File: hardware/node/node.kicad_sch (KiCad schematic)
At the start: 51 parts, among them IC1 MCP73844-840I_MS, IC2 NEO-M9N-00B, J1 USB_C_Receptacle, J2 OMEGA2_HEADER, Q1 IRF7404, Q2 AO3400A, Q3 S8550, SW1 SW_POWER, U1 MT3608, U2 AP63203WU, U3 ADS1115IDGS, U4 Omega2S

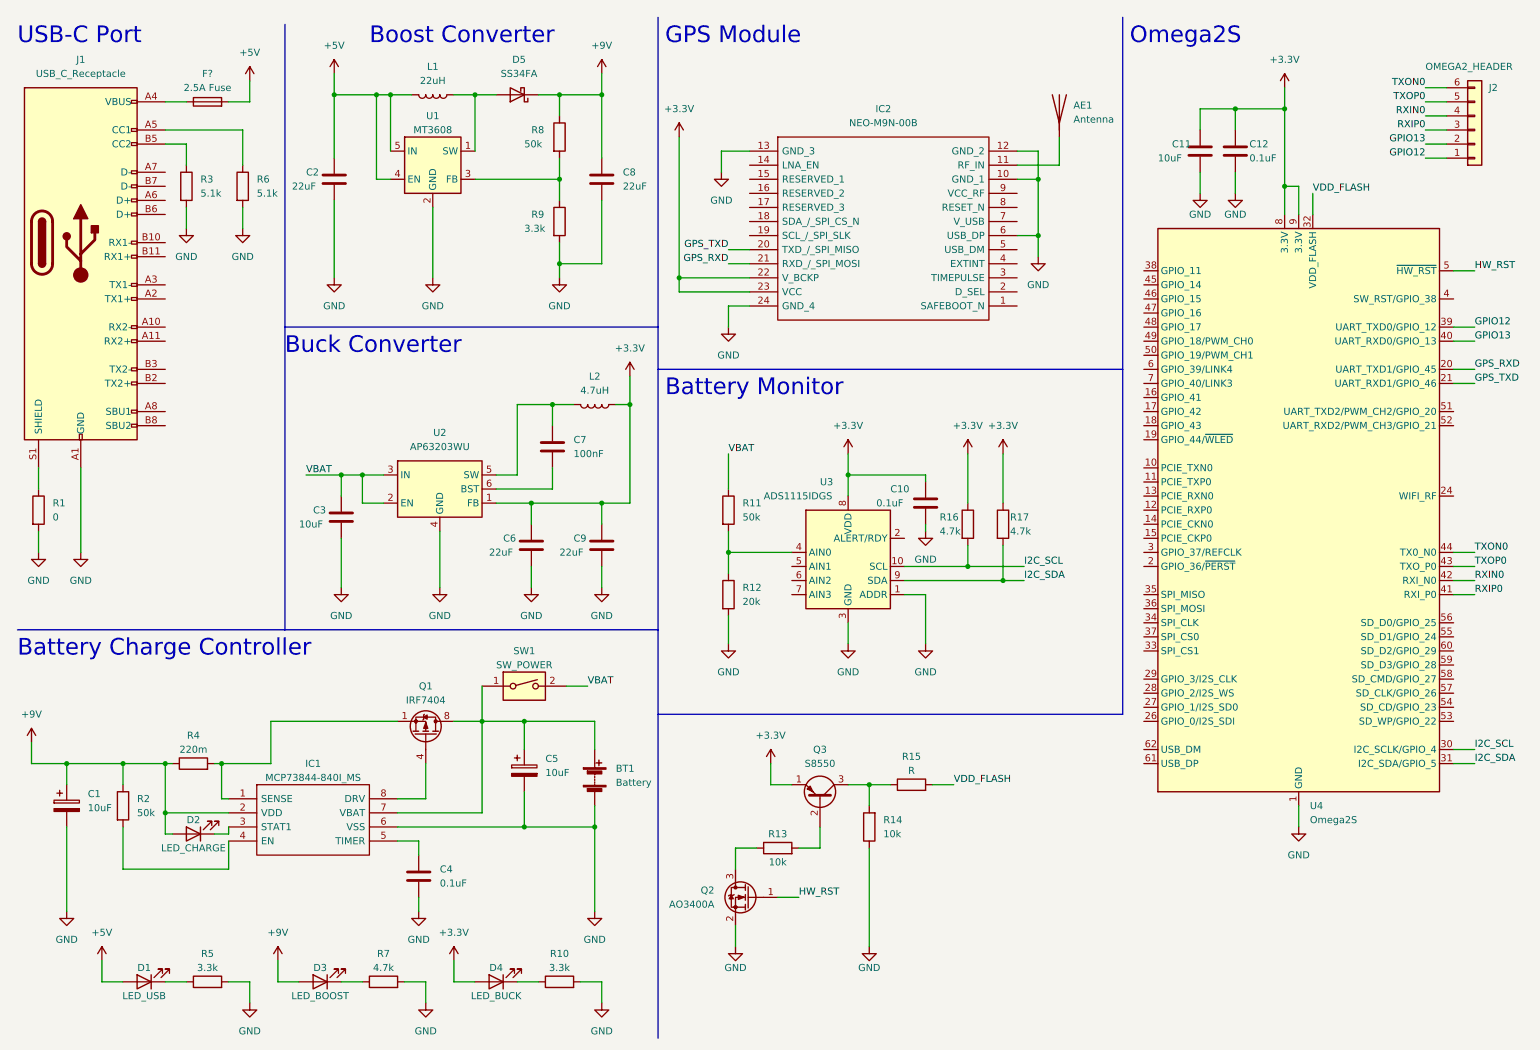
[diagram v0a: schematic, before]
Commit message: fix schematic naming, remove hard reset circuit
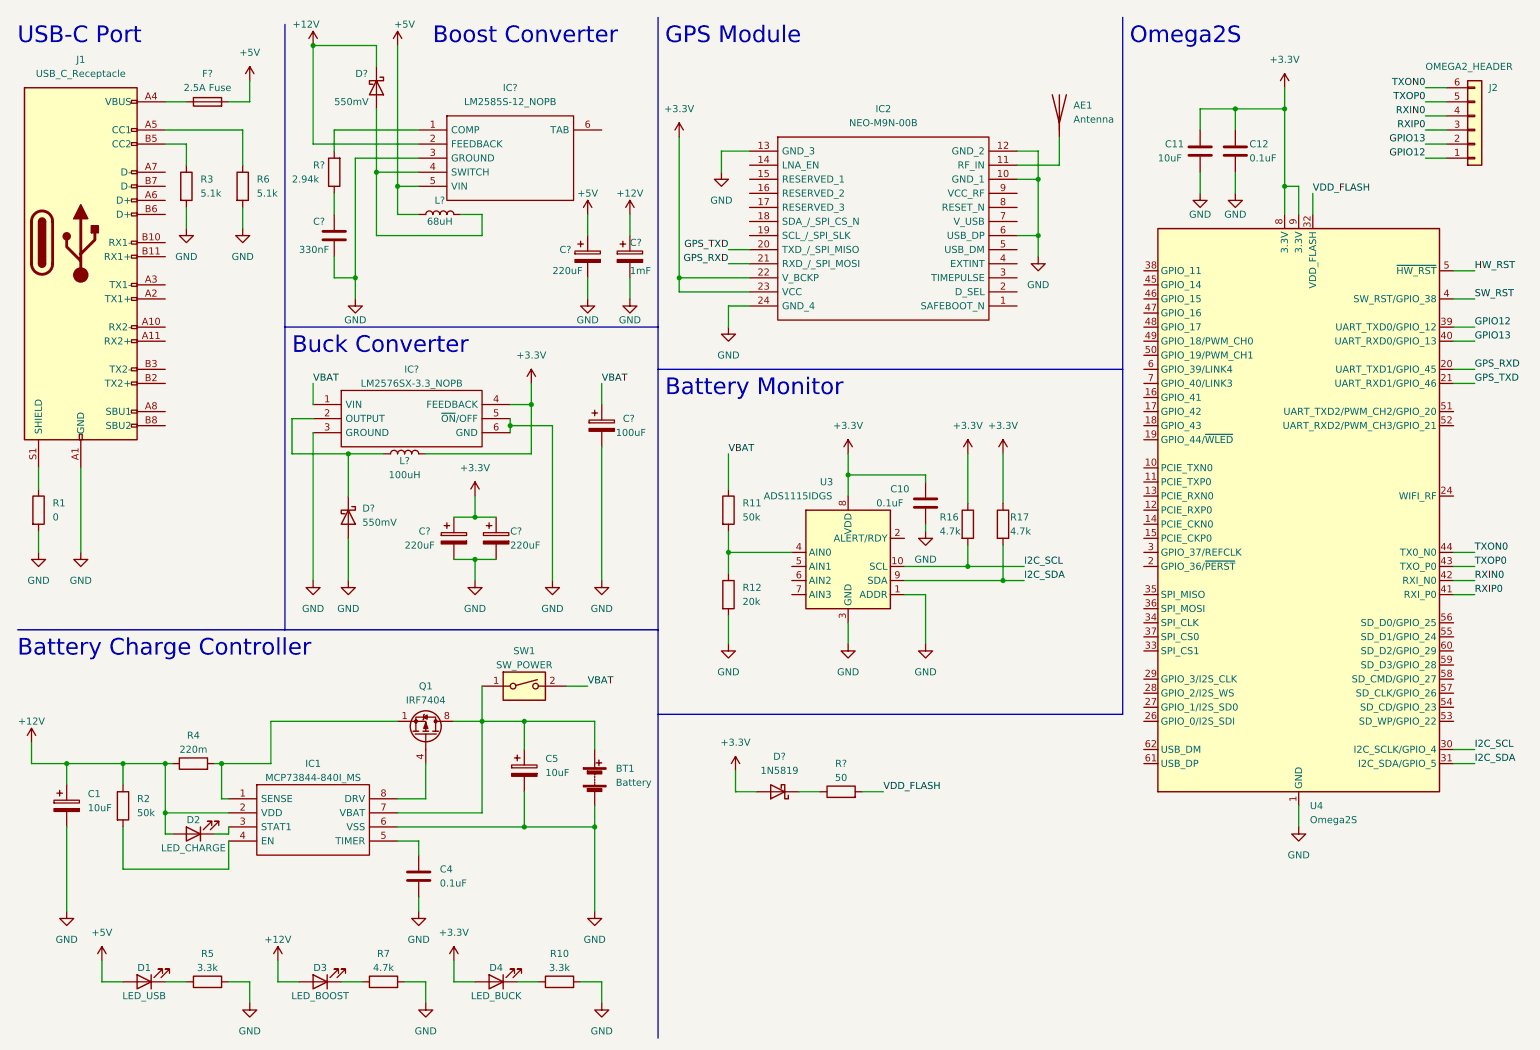
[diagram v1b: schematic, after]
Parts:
- removed C2, C6, C8, C9: 22uF, symbol Device:C
- removed C3: 10uF, symbol Device:C
- removed C7: 100nF, symbol Device:C
- removed D5: SS34FA, symbol Device:D_Schottky
- removed L1: 22uH, symbol Device:L
- removed L2: 4.7uH, symbol Device:L
- removed Q2: AO3400A, Package_TO_SOT_SMD:SOT-23, symbol Transistor_FET:AO3400A
- removed Q3: S8550, Package_TO_SOT_THT:TO-92_Inline, symbol Transistor_BJT:S8550
- removed R13, R14: 10k, symbol Device:R
- removed R15: R, symbol Device:R
- removed R8: 50k, symbol Device:R
- removed R9: 3.3k, symbol Device:R
- removed U1: MT3608, Package_TO_SOT_SMD:SOT-23-6, symbol Regulator_Switching:MT3608
- removed U2: AP63203WU, Package_TO_SOT_SMD:TSOT-23-6, symbol Regulator_Switching:AP63203WU
- added C?: 1mF, symbol Device:C_Polarized
- added C? (x3): 220uF, symbol Device:C_Polarized
- added C?: 100uF, symbol Device:C_Polarized
- added C?: 330nF, symbol Device:C
- added D? (x2): 550mV, symbol Device:D_Schottky
- added D?: 1N5819, Diode_THT:D_DO-41_SOD81_P10.16mm_Horizontal, symbol Diode:1N5819
- added IC?: LM2585S-12_NOPB, TO170P1435X465-6N, symbol Boost_Converter_12v:LM2585S-12_NOPB
- added IC?: LM2576SX-3.3_NOPB, KTT0005B, symbol Buck_Converter:LM2576SX-3.3_NOPB
- added L?: 68uH, symbol Device:L
- added L?: 100uH, symbol Device:L
- added R?: 2.94k, symbol Device:R
- added R?: 50, symbol Device:R
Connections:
- net +3.3V: now also C?.1, C?.1, D?.2 (A), IC?.4 (FEEDBACK), L?.2
- net +5V: now also C?.1, IC?.5 (VIN), L?.1
- net GND: now also C?.2, C?.2, C?.2, C?.2, C?.2, C?.2, D?.2 (A), IC?.3 (GROUND), IC?.3 (GROUND), IC?.5 (~{ON}/OFF), IC?.6 (GND)
- net VBAT: now also C?.1, IC?.1 (VIN)
- net VDD_FLASH: now also R?.2
- net SW_RST: now reaches U4.4 (SW_RST/GPIO_38)
- net +9V renamed +12V
- net +12V: now also C?.1, D?.1 (K), IC?.2 (FEEDBACK)
- new net: D?.2 (A), IC?.4 (SWITCH), L?.2
- new net: IC?.1 (COMP), R?.2
- new net: C?.1, R?.1
- new net: D?.1 (K), IC?.2 (OUTPUT), L?.1
- new net: D?.1 (K), R?.1

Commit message: push latest hardware changes (TODO: active GPS antenna)
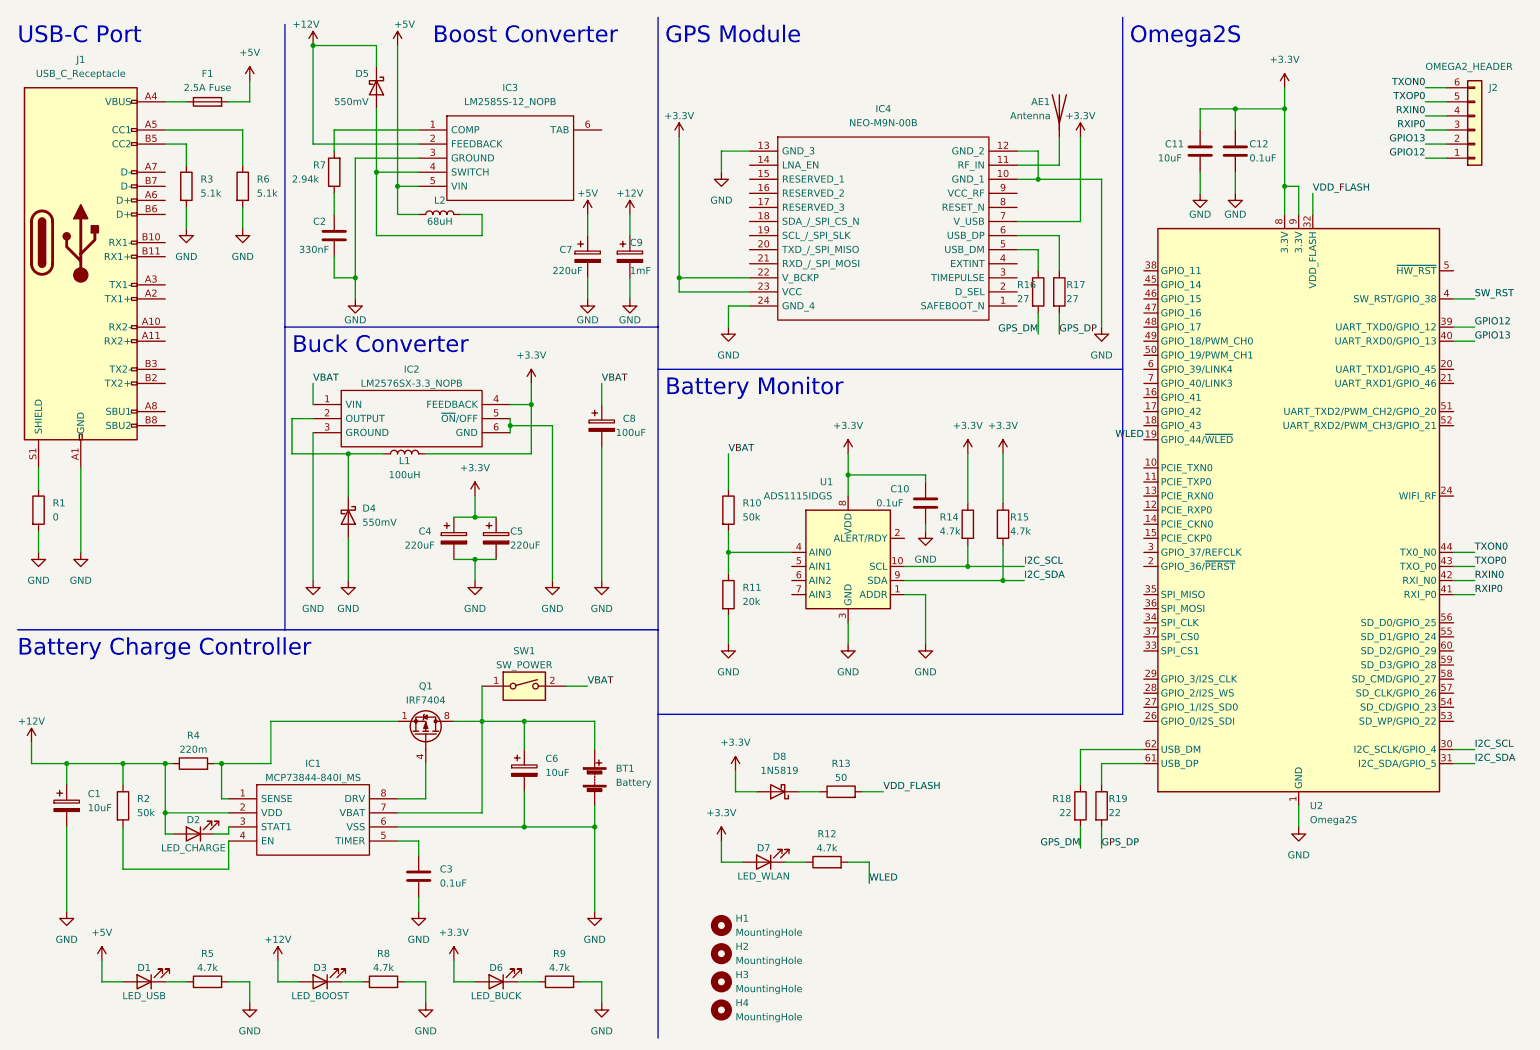
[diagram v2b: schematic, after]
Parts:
- added D7: LED_WLAN, symbol Device:LED
- added H1, H2, H3, H4: MountingHole, symbol Mechanical:MountingHole
- added R12: 4.7k, symbol Device:R
- added R16, R17: 27, symbol Device:R
- added R18, R19: 22, symbol Device:R
- R5: value 3.3k -> 4.7k
- R9: renamed from R10; value 3.3k -> 4.7k
- gave numbers to parts that had none: 16
- renumbered C4 to C3, C5 to C6, D4 to D6, IC2 to IC4, R11 to R10, R12 to R11, R16 to R14, R17 to R15, R7 to R8, U3 to U1, U4 to U2
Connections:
- net +3.3V: now also IC4.7 (V_USB), D7.2 (A)
- net GND: no longer IC4.6 (USB_DP)
- net WLED: now reaches U2.19 (GPIO_44/~{WLED})
- net WLED: now also R12.2
- net at U2.61 (USB_DP): now also R19.1
- net at U2.62 (USB_DM): now also R18.1
- net at IC4.5 (USB_DM): now also R16.1
- net GPS_RXD: no longer names the net of U2.20 (UART_TXD1/GPIO_45)
- net GPS_RXD: no longer IC4.21 (RXD_/_SPI_MOSI)
- net GPS_TXD: no longer names the net of U2.21 (UART_RXD1/GPIO_46)
- net GPS_TXD: no longer IC4.20 (TXD_/_SPI_MISO)
- net HW_RST: no longer names the net of U2.5 (~{HW_RST})
- new net: D7.1 (K), R12.1
- new net: IC4.6 (USB_DP), R17.1
- new net GPS_DM: R16.2, R18.2
- new net GPS_DP: R17.2, R19.2

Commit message: import component footprints / symbols
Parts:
- removed AE1: Antenna, symbol Device:Antenna
- removed BT1: Battery, symbol Device:Battery
- removed D3: LED_BOOST, symbol Device:LED
- removed J1: USB_C_Receptacle, symbol Connector:USB_C_Receptacle
- removed R8: 4.7k, symbol Device:R
- added C?: 47pF, symbol Device:C
- added D?: LED_GPS, symbol Device:LED
- added J?: U.FL-R-SMT_01_, UFLRSMT01, symbol U.FL-R-SMT_01_:U.FL-R-SMT_01_
- added J?: USB4135-GF-A, USB4135GFA, symbol USB4135-GF-A:USB4135-GF-A
- added J?: 2x18650, 1123, symbol 1123:1123
- added L?: 30R/1.8A, symbol Device:L_Iron
- added R?: 1k, symbol Device:R
- added R?: 10, symbol Device:R
- R12, R5, R9: value 4.7k -> 1k
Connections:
- net GND: now also R1.1, C?.2, D?.1 (K), J?.1, J?.1 (GND_1), J?.2 (GND_2), J?.A12, J?.B12; no longer R1.2
- net at C6.1, IC1.7 (VBAT), Q1.5 (D)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: now also J?.3
- net at R3.1: now also J?.A5
- net at R6.1: now also J?.B5
- net GPS_ANT: now reaches IC4.11 (RF_IN)
- net GPS_ANT: now also J?.3 (SIG), L?.1
- net at F1.1: now also J?.A9, J?.B9
- net at IC4.3 (TIMEPULSE): now also R?.2
- net VCC_RF: now reaches IC4.9 (VCC_RF)
- net VCC_RF: now also R?.2
- new net: J?.MP1, J?.MP2, J?.MP3, J?.MP4, R1.2
- new net: D?.2 (A), R?.1
- new net: C?.1, L?.2, R?.1
- new net: J?.2, J?.4
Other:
- moved on the sheet: D7, D8, F1, H1, H2, H3, H4, R1, R12, R13, R16, R17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

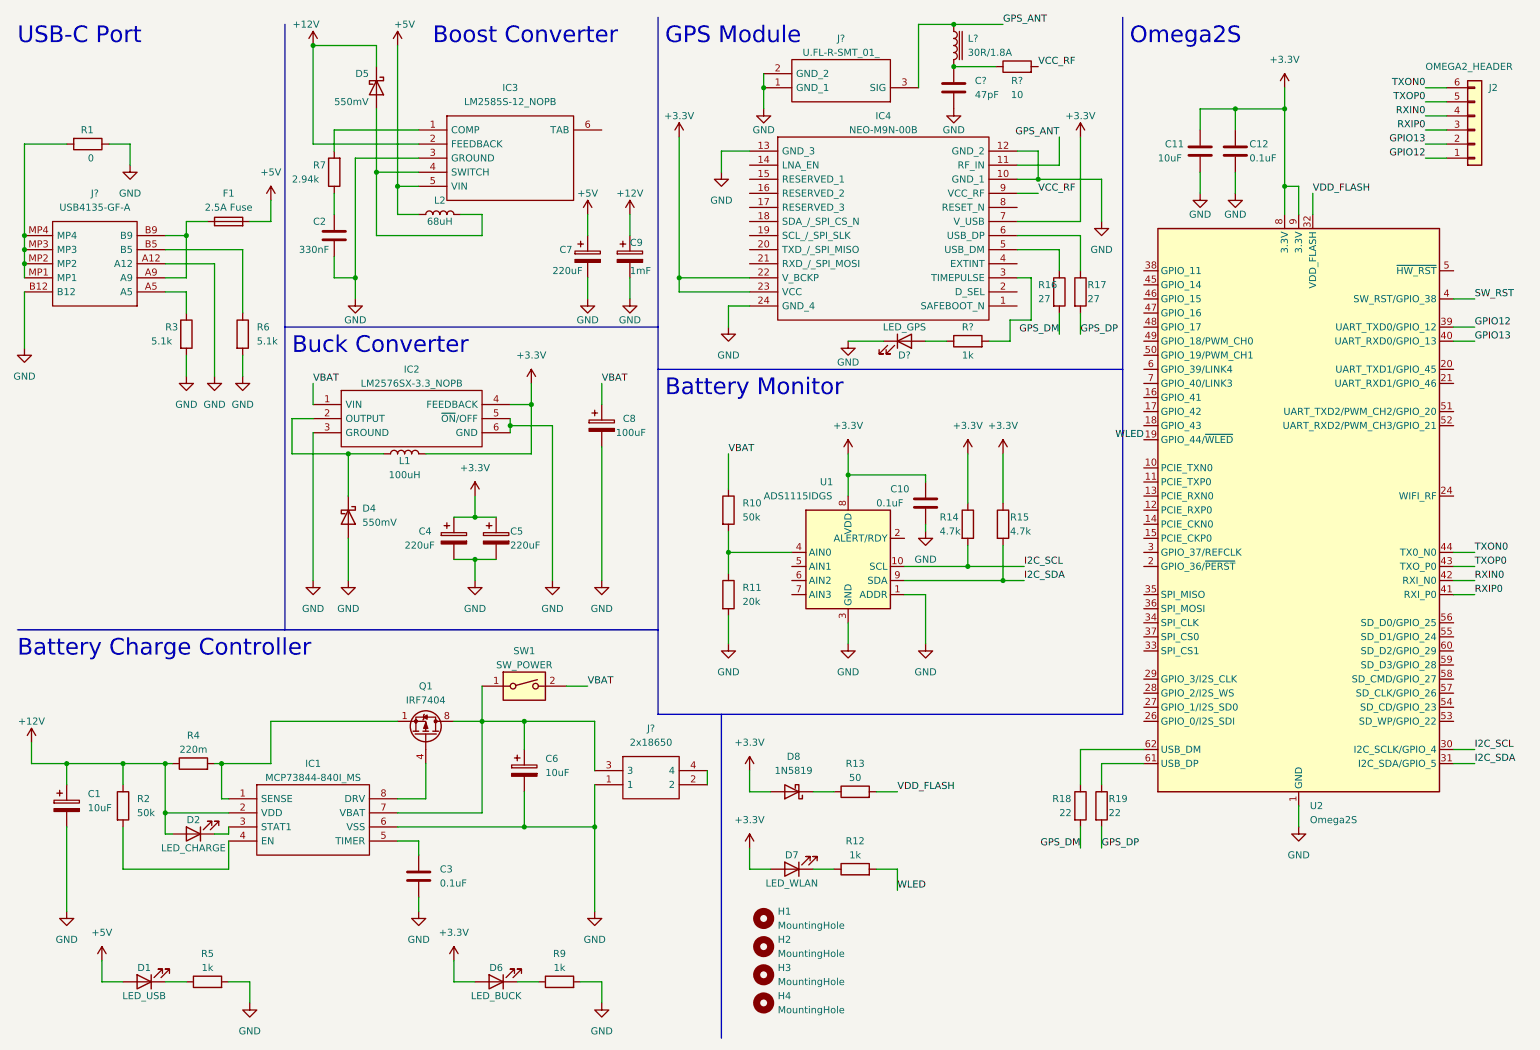
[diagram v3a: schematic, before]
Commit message: finish capacitor part selection and footprint assignment
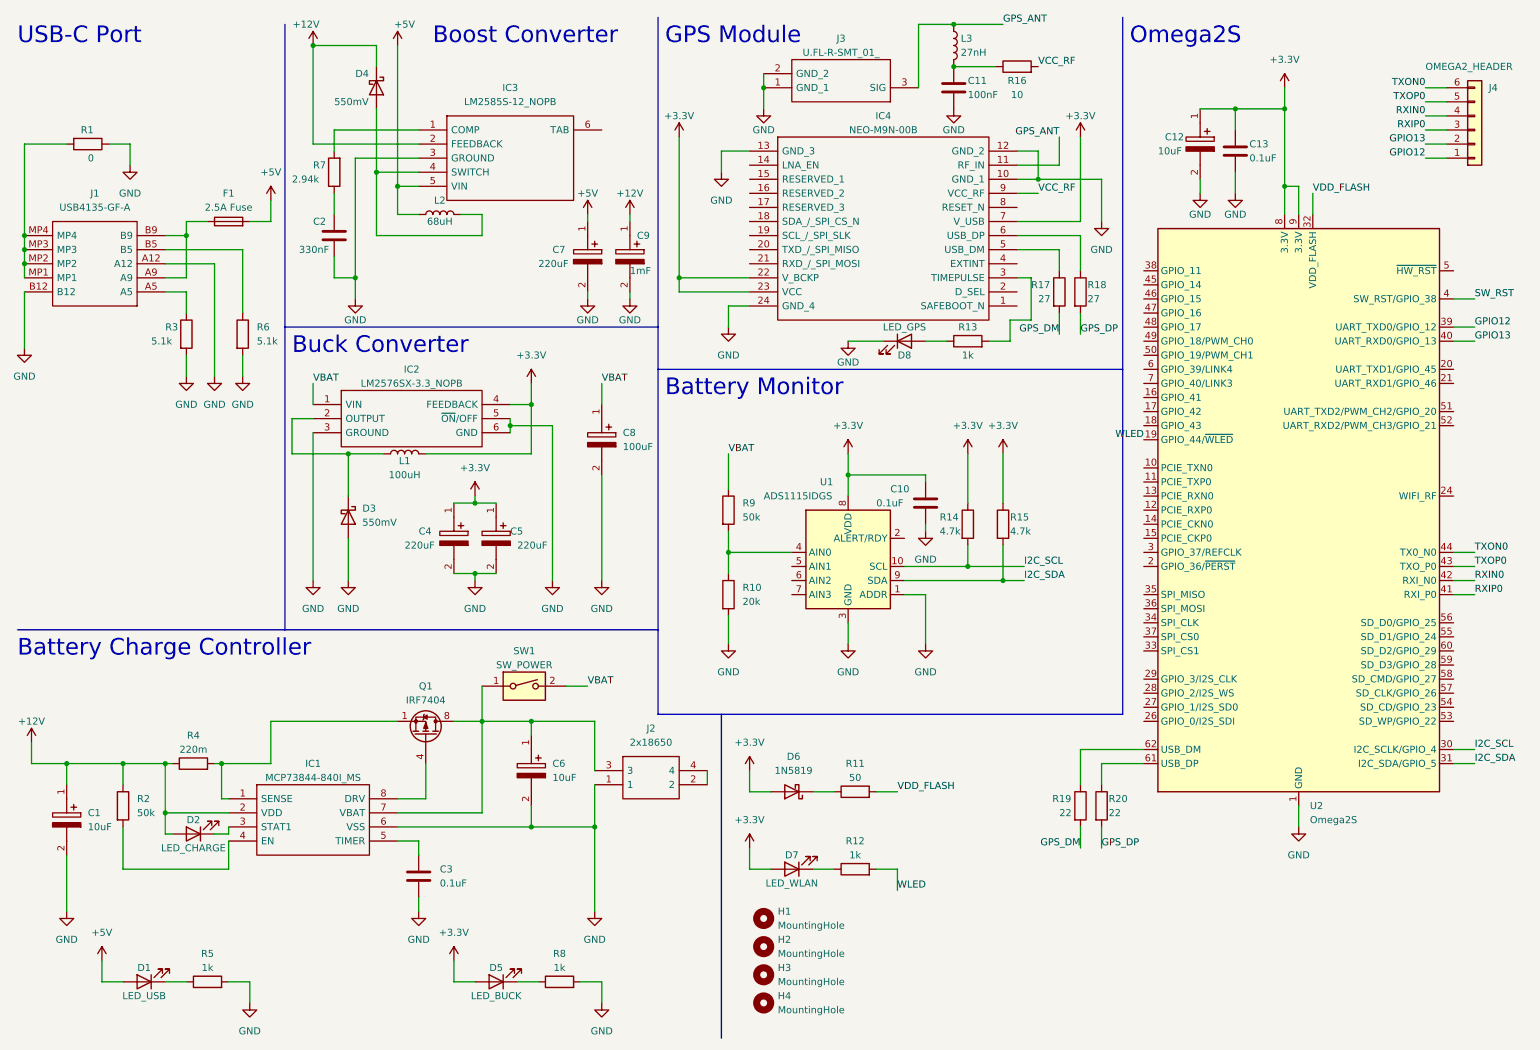
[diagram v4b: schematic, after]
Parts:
- removed C1, C6: 10uF, symbol Device:C_Polarized
- removed C11: 10uF, symbol Device:C
- removed C4, C5, C7: 220uF, symbol Device:C_Polarized
- removed C8: 100uF, symbol Device:C_Polarized
- removed C9: 1mF, symbol Device:C_Polarized
- removed L?: 30R/1.8A, symbol Device:L_Iron
- added C1, C12, C6: 10uF, EEE1AA220WR, symbol EEE-FN1E100R:EEE-FN1E100R
- added C4, C5, C7: 220uF, CAPAE660X800N, symbol UUD1C221MCL1GS:UUD1C221MCL1GS
- added C8: 100uF, 16SVF180M, symbol 16SVPC100M:16SVPC100M
- added C9: 1mF, 16SVF1000M, symbol 16SVPF1000M:16SVPF1000M
- added L3: 27nH, symbol Device:L
- C10, C2, C3: footprint (none) -> Capacitor_SMD:C_1206_3216Metric_Pad1.33x1.80mm_HandSolder
- C11: renamed from C?; value 47pF -> 100nF
- C13: renamed from C12; footprint (none) -> Capacitor_SMD:C_1206_3216Metric_Pad1.33x1.80mm_HandSolder
- gave numbers to parts that had none: 6
- renumbered D4 to D3, D5 to D4, D6 to D5, D8 to D6, J2 to J4, R11 to R10, R13 to R11, R16 to R17, R17 to R18, R18 to R19, R19 to R20, R9 to R8, R10 to R9
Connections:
- net +12V: now also C1.1, C9.1
- net +3.3V: now also C12.1, C4.1, C5.1
- net +5V: now also C7.1
- net GND: now also C1.2, C12.2, C4.2, C5.2, C6.2, C7.2, C8.2, C9.2
- net GPS_ANT: now also L3.1
- net VBAT: now also C8.1
- net at IC1.7 (VBAT), J2.3, Q1.5 (D)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: now also C6.1
- net at C11.1, R16.1: now also L3.2
